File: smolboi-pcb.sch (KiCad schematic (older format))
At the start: 17 parts, among them U1 STM32F103C8Tx

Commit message: schematic before check
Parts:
- removed J?: USB_C_Receptacle_USB2.0, symbol Connector:USB_C_Receptacle_USB2.0
- added C? (x2): 1uF, symbol Device:C_Small
- added U?: XC6206, symbol random-keyboard-parts:XC6206
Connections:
- wire segments 80 -> 86
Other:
- note added: "USB_C Connector with ESD Protection"
- note added: "Voltage Step Down"
- moved on the sheet: C1, C2, C3, C4, C5, F?, R?, SW?, U1, U?, USB?

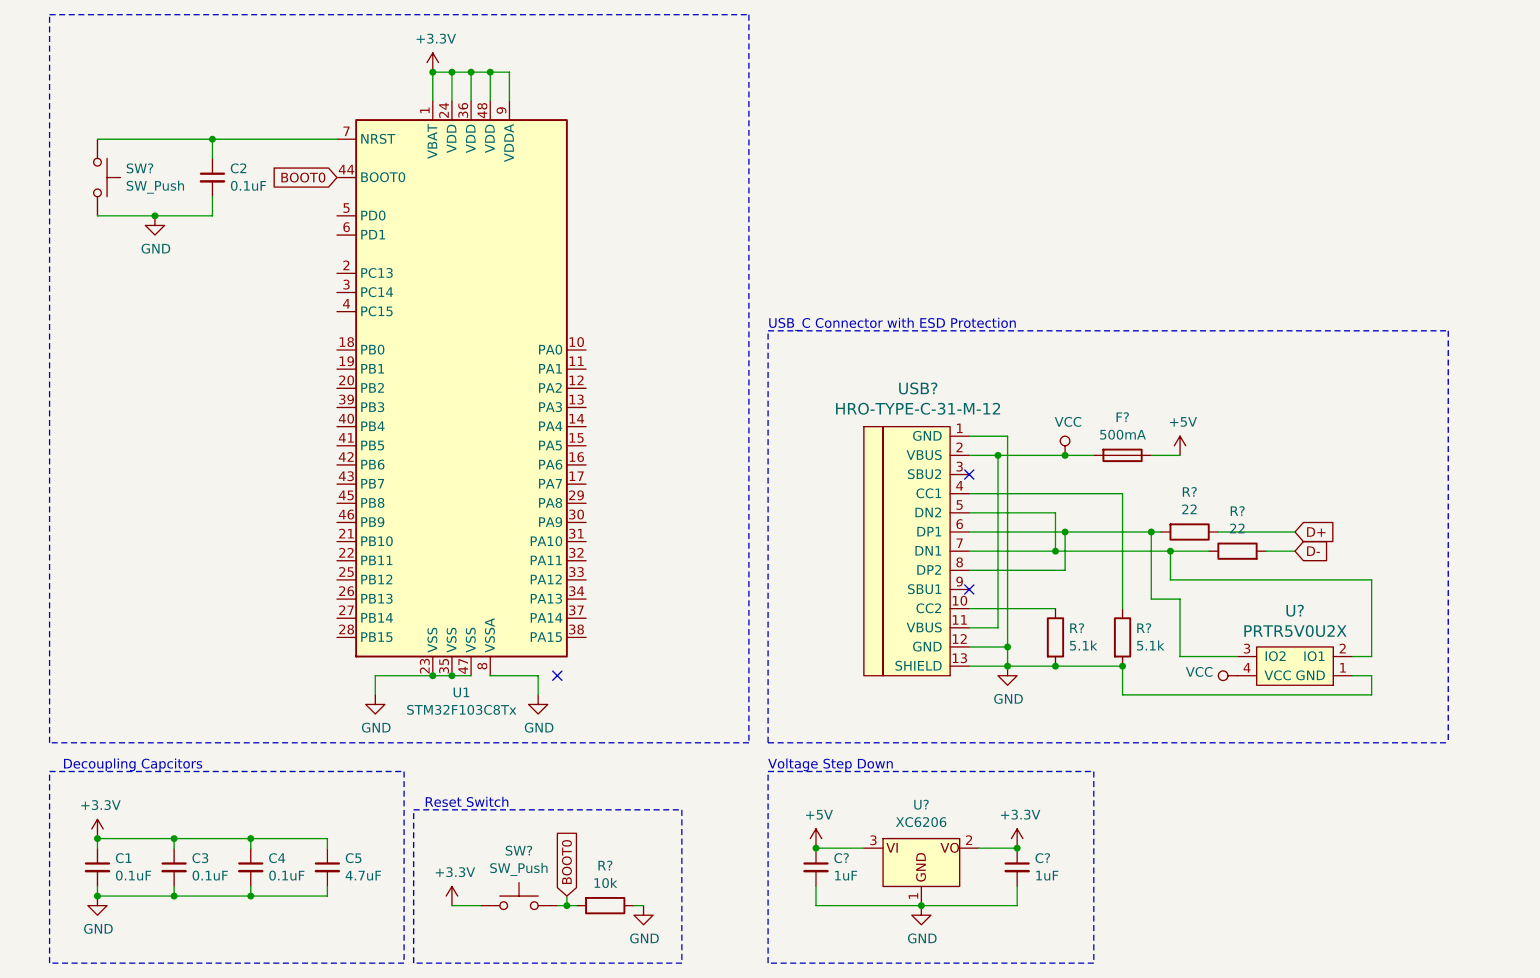
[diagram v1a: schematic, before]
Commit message: ceramic oscillator, major schematic modules finalized
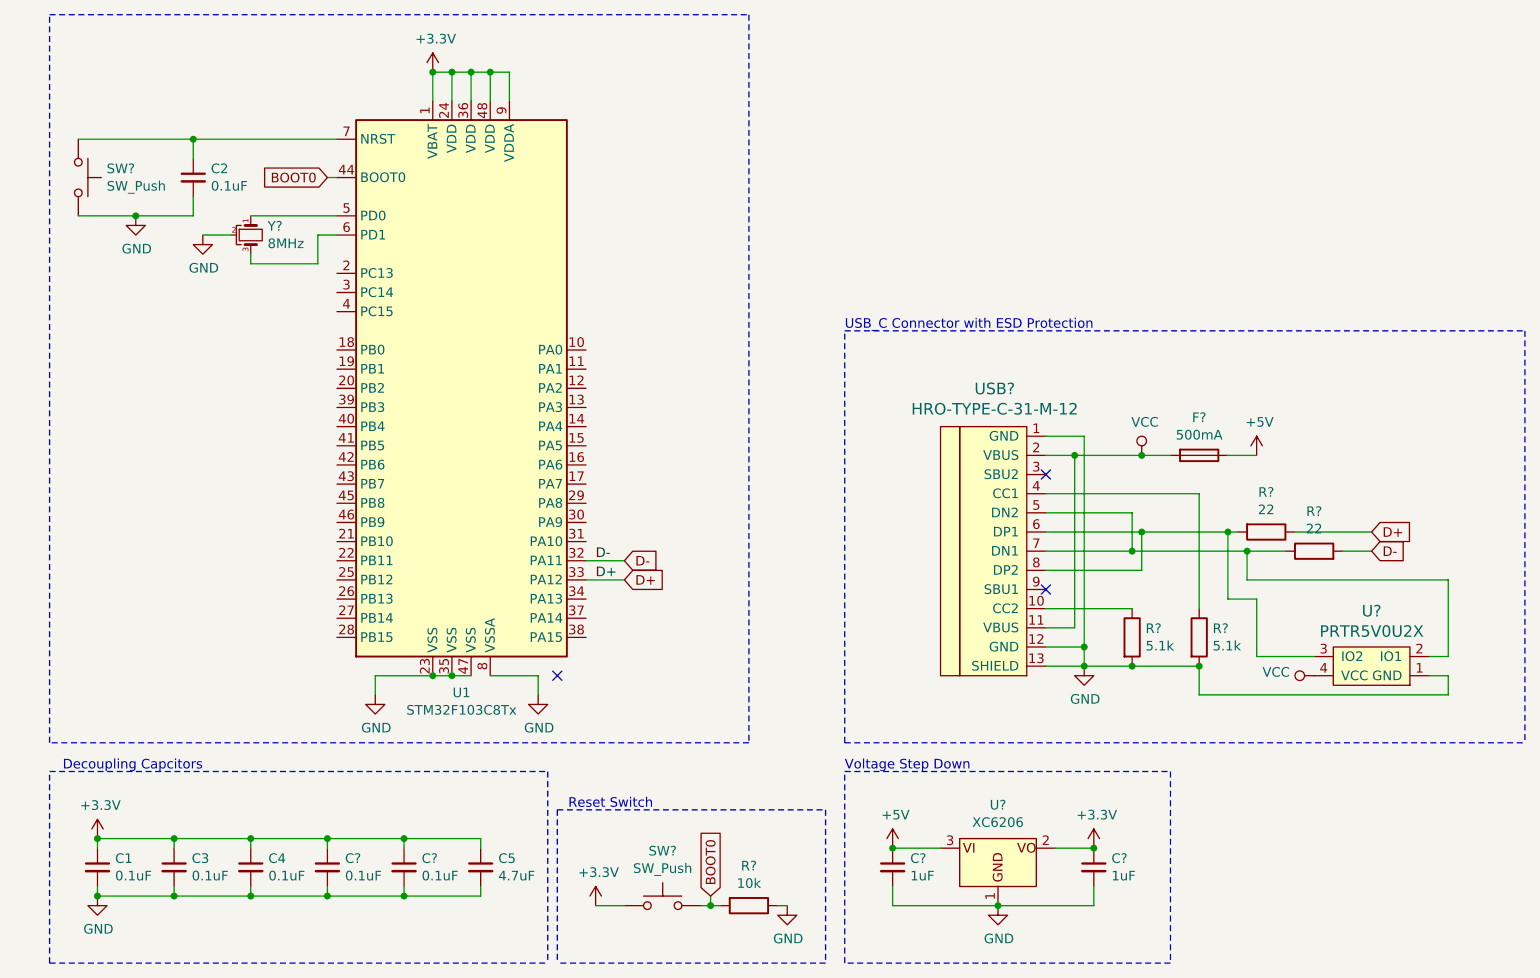
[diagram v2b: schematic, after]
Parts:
- added C? (x2): 0.1uF, symbol Device:C_Small
- added Y?: 8MHz, symbol Device:Crystal_GND2_Small
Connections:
- net +3V3: now also C?.1, C?.1
- net D+: now also U1.33 (PA12)
- net D-: now also U1.32 (PA11)
- net GND: now also C?.2, C?.2, Y?.2
- net at U1.5 (PD0): now also Y?.1
- net at U1.6 (PD1): now also Y?.3
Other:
- moved on the sheet: C2, C5, C?, F?, R?, SW?, U?, USB?

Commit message: up to finish diff pair routing
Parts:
- added D1, D10, D11, D12, D13, D14, D15, D16, D17, D18, D19, D2, D20, D21, D22, D23, D24, D25, D26, D27, D28, D29, D3, D30, D31, D32, D33, D34, D35, D36, D37, D38, D39, D4, D40, D41, D42, D43, D44, D45, D46, D5, D6, D7, D8, D9: D, Diode_SMD:D_SOD-123, symbol Device:D
- added SW1: ESC, MX_Only:MXOnly-1U-Hotswap, symbol Switch:SW_Push
- added SW10: O, MX_Only:MXOnly-1U-Hotswap, symbol Switch:SW_Push
- added SW11: P, MX_Only:MXOnly-1U-Hotswap, symbol Switch:SW_Push
- added SW12: Bksp, MX_Only:MXOnly-1U-Hotswap, symbol Switch:SW_Push
- added SW13: Tab, MX_Only:MXOnly-1U-Hotswap, symbol Switch:SW_Push
- added SW14: A, MX_Only:MXOnly-1U-Hotswap, symbol Switch:SW_Push
- added SW15: S, MX_Only:MXOnly-1U-Hotswap, symbol Switch:SW_Push
- added SW16: D, MX_Only:MXOnly-1U-Hotswap, symbol Switch:SW_Push
- added SW17: F, MX_Only:MXOnly-1U-Hotswap, symbol Switch:SW_Push
- added SW18: G, MX_Only:MXOnly-1U-Hotswap, symbol Switch:SW_Push
- added SW19: H, MX_Only:MXOnly-1U-Hotswap, symbol Switch:SW_Push
- added SW2: Q, MX_Only:MXOnly-1U-Hotswap, symbol Switch:SW_Push
- added SW20: J, MX_Only:MXOnly-1U-Hotswap, symbol Switch:SW_Push
- added SW21: K, MX_Only:MXOnly-1U-Hotswap, symbol Switch:SW_Push
- added SW22: L, MX_Only:MXOnly-1U-Hotswap, symbol Switch:SW_Push
- added SW23: ;, MX_Only:MXOnly-1U-Hotswap, symbol Switch:SW_Push
- added SW24: ', MX_Only:MXOnly-1U-Hotswap, symbol Switch:SW_Push
- added SW25: Shift, MX_Only:MXOnly-1U-Hotswap, symbol Switch:SW_Push
- added SW26: Z, MX_Only:MXOnly-1U-Hotswap, symbol Switch:SW_Push
- added SW27: X, MX_Only:MXOnly-1U-Hotswap, symbol Switch:SW_Push
- added SW28: C, MX_Only:MXOnly-1U-Hotswap, symbol Switch:SW_Push
- added SW29: V, MX_Only:MXOnly-1U-Hotswap, symbol Switch:SW_Push
- added SW3: W, MX_Only:MXOnly-1U-Hotswap, symbol Switch:SW_Push
- added SW30: B, MX_Only:MXOnly-1U-Hotswap, symbol Switch:SW_Push
- added SW31: N, MX_Only:MXOnly-1U-Hotswap, symbol Switch:SW_Push
- added SW32: M, MX_Only:MXOnly-1U-Hotswap, symbol Switch:SW_Push
- added SW33: ,, MX_Only:MXOnly-1U-Hotswap, symbol Switch:SW_Push
- added SW34: ., MX_Only:MXOnly-1U-Hotswap, symbol Switch:SW_Push
- added SW35: /, MX_Only:MXOnly-1U-Hotswap, symbol Switch:SW_Push
- added SW36: CpsLk, MX_Only:MXOnly-1U-Hotswap, symbol Switch:SW_Push
- added SW37: Ctrl, MX_Only:MXOnly-1U-Hotswap, symbol Switch:SW_Push
- added SW38: Win, MX_Only:MXOnly-1U-Hotswap, symbol Switch:SW_Push
- added SW39: Alt, MX_Only:MXOnly-1U-Hotswap, symbol Switch:SW_Push
- added SW4: E, MX_Only:MXOnly-1U-Hotswap, symbol Switch:SW_Push
- added SW40: FUP, MX_Only:MXOnly-1U-Hotswap, symbol Switch:SW_Push
- added SW41: FDN, MX_Only:MXOnly-1U-Hotswap, symbol Switch:SW_Push
- added SW42: Space, MX_Only:MXOnly-3U-Hotswap, symbol Switch:SW_Push
- added SW43: FRI, MX_Only:MXOnly-1U-Hotswap, symbol Switch:SW_Push
- added SW44: Left, MX_Only:MXOnly-1U-Hotswap, symbol Switch:SW_Push
- added SW45: Del, MX_Only:MXOnly-1U-Hotswap, symbol Switch:SW_Push
- added SW46: Enter, MX_Only:MXOnly-1U-Hotswap, symbol Switch:SW_Push
- added SW5: R, MX_Only:MXOnly-1U-Hotswap, symbol Switch:SW_Push
- added SW6: T, MX_Only:MXOnly-1U-Hotswap, symbol Switch:SW_Push
- added SW7: Y, MX_Only:MXOnly-1U-Hotswap, symbol Switch:SW_Push
- added SW8: U, MX_Only:MXOnly-1U-Hotswap, symbol Switch:SW_Push
- added SW9: I, MX_Only:MXOnly-1U-Hotswap, symbol Switch:SW_Push
- C1: renamed from C2; footprint (none) -> Capacitor_SMD:C_0402_1005Metric
- C2: renamed from C1; footprint (none) -> Capacitor_SMD:C_0402_1005Metric
- C3, C4: footprint (none) -> Capacitor_SMD:C_0402_1005Metric
- C5, C6, C8, C9: renamed from C?; footprint (none) -> Capacitor_SMD:C_0402_1005Metric
- C7: renamed from C5; footprint (none) -> Capacitor_SMD:C_0402_1005Metric
- F1: renamed from F?; footprint (none) -> Fuse:Fuse_1206_3216Metric
- R1, R2, R3, R4, R5: renamed from R?; footprint (none) -> Resistor_SMD:R_0402_1005Metric
- SW47, SW48: renamed from SW?; footprint (none) -> Button_Switch_SMD:SW_SPST_SKQG_WithStem
- U2: renamed from U?; footprint (none) -> random-keyboard-parts:SOT143B
- U3: renamed from U?; footprint (none) -> PMIC-LDO-XC6206P332MR-G_SOT23_:SOT-23
- USB1: renamed from USB?; footprint (none) -> Type-C:HRO-TYPE-C-31-M-12-Assembly
- Y1: renamed from Y?; footprint (none) -> CSTNE8M00GH5C000R0:OSC_CSTNE8M00GH5C000R0
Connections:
- net DN: now reaches R2.1, USB1.5 (DN2), USB1.7 (DN1)
- net DN: now also U2.3 (IO2); no longer U2.2 (IO1)
- net DP: now reaches R1.2, USB1.6 (DP1), USB1.8 (DP2)
- net DP: now also U2.2 (IO1); no longer U2.3 (IO2)
- new net: D1.2 (A), SW1.1
- new net: D2.2 (A), SW2.1
- new net: D3.2 (A), SW3.1
- new net: D4.2 (A), SW4.1
- new net: D5.2 (A), SW5.1
- new net: D6.2 (A), SW6.1
- new net: D7.2 (A), SW7.1
- new net: D8.2 (A), SW8.1
- new net: D9.2 (A), SW9.1
- new net: D10.2 (A), SW10.1
- new net: D11.2 (A), SW11.1
- new net: D12.2 (A), SW12.1
- new net: D13.2 (A), SW13.1
- new net: D14.2 (A), SW14.1
- new net: D15.2 (A), SW15.1
- new net: D16.2 (A), SW16.1
- new net: D17.2 (A), SW17.1
- new net: D18.2 (A), SW18.1
- new net: D19.2 (A), SW19.1
- new net: D20.2 (A), SW20.1
- new net: D21.2 (A), SW21.1
- new net: D22.2 (A), SW22.1
- new net: D23.2 (A), SW23.1
- new net: D24.2 (A), SW24.1
- new net: D25.2 (A), SW25.1
- new net: D26.2 (A), SW26.1
- new net: D27.2 (A), SW27.1
- new net: D28.2 (A), SW28.1
- new net: D29.2 (A), SW29.1
- new net: D30.2 (A), SW30.1
- new net: D31.2 (A), SW31.1
- new net: D32.2 (A), SW32.1
- new net: D33.2 (A), SW33.1
- new net: D34.2 (A), SW34.1
- new net: D35.2 (A), SW35.1
- new net: D36.2 (A), SW36.1
- new net: D37.2 (A), SW37.1
- new net: D38.2 (A), SW38.1
- new net: D39.2 (A), SW39.1
- new net: D40.2 (A), SW40.1
- new net: D41.2 (A), SW41.1
- new net: D42.2 (A), SW42.1
- new net: D43.2 (A), SW43.1
- new net: D44.2 (A), SW44.1
- new net: D45.2 (A), SW45.1
- new net: D46.2 (A), SW46.1
- new net col0: SW1.2, SW13.2, SW25.2, SW37.2
- new net col1: SW14.2, SW2.2, SW26.2, SW38.2
- new net col10: SW11.2, SW23.2, SW35.2, SW45.2
- new net col11: SW12.2, SW24.2, SW36.2, SW46.2
- new net col2: SW15.2, SW27.2, SW3.2, SW39.2
- new net col3: SW16.2, SW28.2, SW4.2, SW40.2
- new net col4: SW17.2, SW29.2, SW41.2, SW5.2
- new net col5: SW18.2, SW30.2, SW6.2
- new net col6: SW19.2, SW31.2, SW42.2, SW7.2
- new net col7: SW20.2, SW32.2, SW8.2
- new net col8: SW21.2, SW33.2, SW43.2, SW9.2
- new net col9: SW10.2, SW22.2, SW34.2, SW44.2
- new net row0: D1.1 (K), D10.1 (K), D11.1 (K), D12.1 (K), D2.1 (K), D3.1 (K), D4.1 (K), D5.1 (K), D6.1 (K), D7.1 (K), D8.1 (K), D9.1 (K)
- new net row1: D13.1 (K), D14.1 (K), D15.1 (K), D16.1 (K), D17.1 (K), D18.1 (K), D19.1 (K), D20.1 (K), D21.1 (K), D22.1 (K), D23.1 (K), D24.1 (K)
- new net row2: D25.1 (K), D26.1 (K), D27.1 (K), D28.1 (K), D29.1 (K), D30.1 (K), D31.1 (K), D32.1 (K), D33.1 (K), D34.1 (K), D35.1 (K), D36.1 (K)
- new net row3: D37.1 (K), D38.1 (K), D39.1 (K), D40.1 (K), D41.1 (K), D42.1 (K), D43.1 (K), D44.1 (K), D45.1 (K), D46.1 (K)
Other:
- note added: "08-21-2024"
- note added: "1.0\n"
- note added: "Smolboi PCB"
- moved on the sheet: C1, C2, C3, C4, C5, C6, C7, C8, C9, F1, R1, R2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

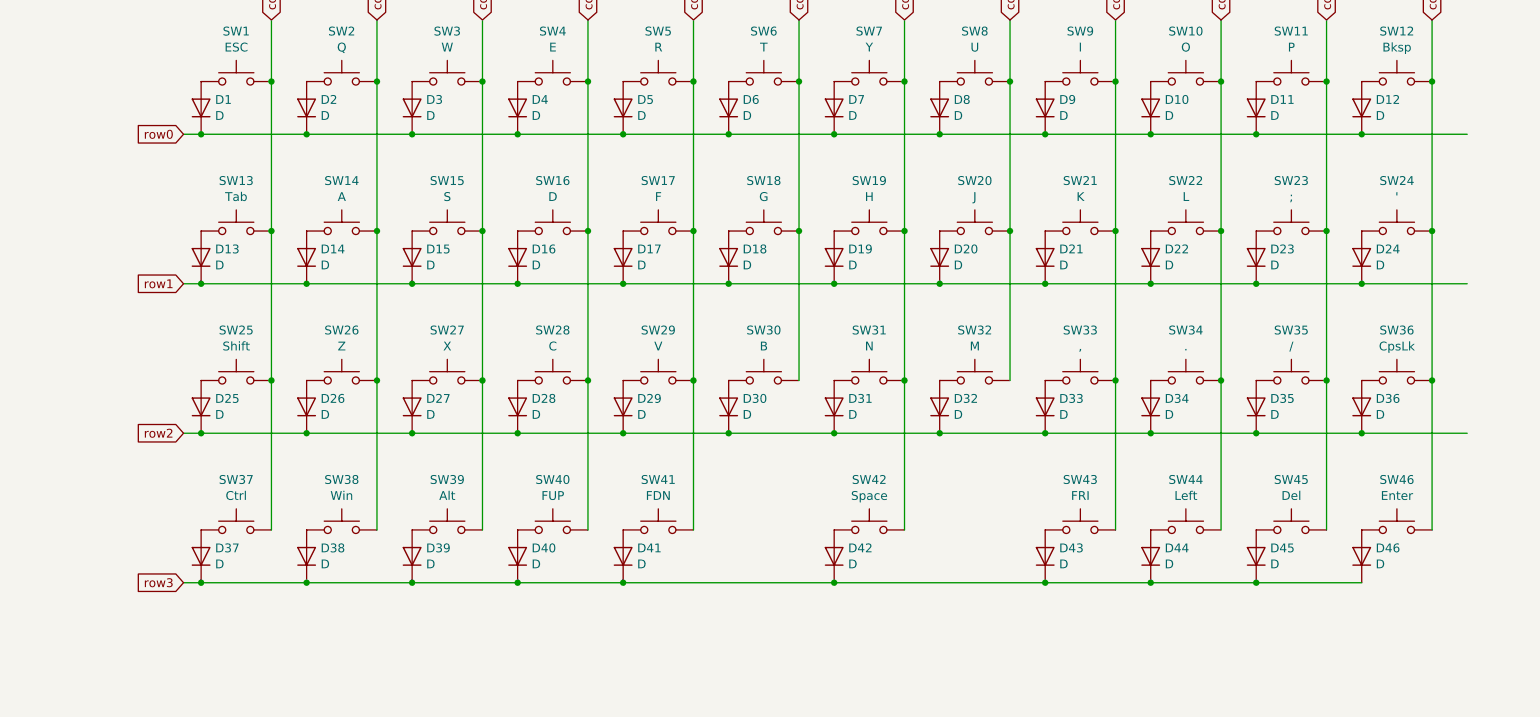
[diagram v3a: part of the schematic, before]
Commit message: staggered layout, routed diff pair on right side
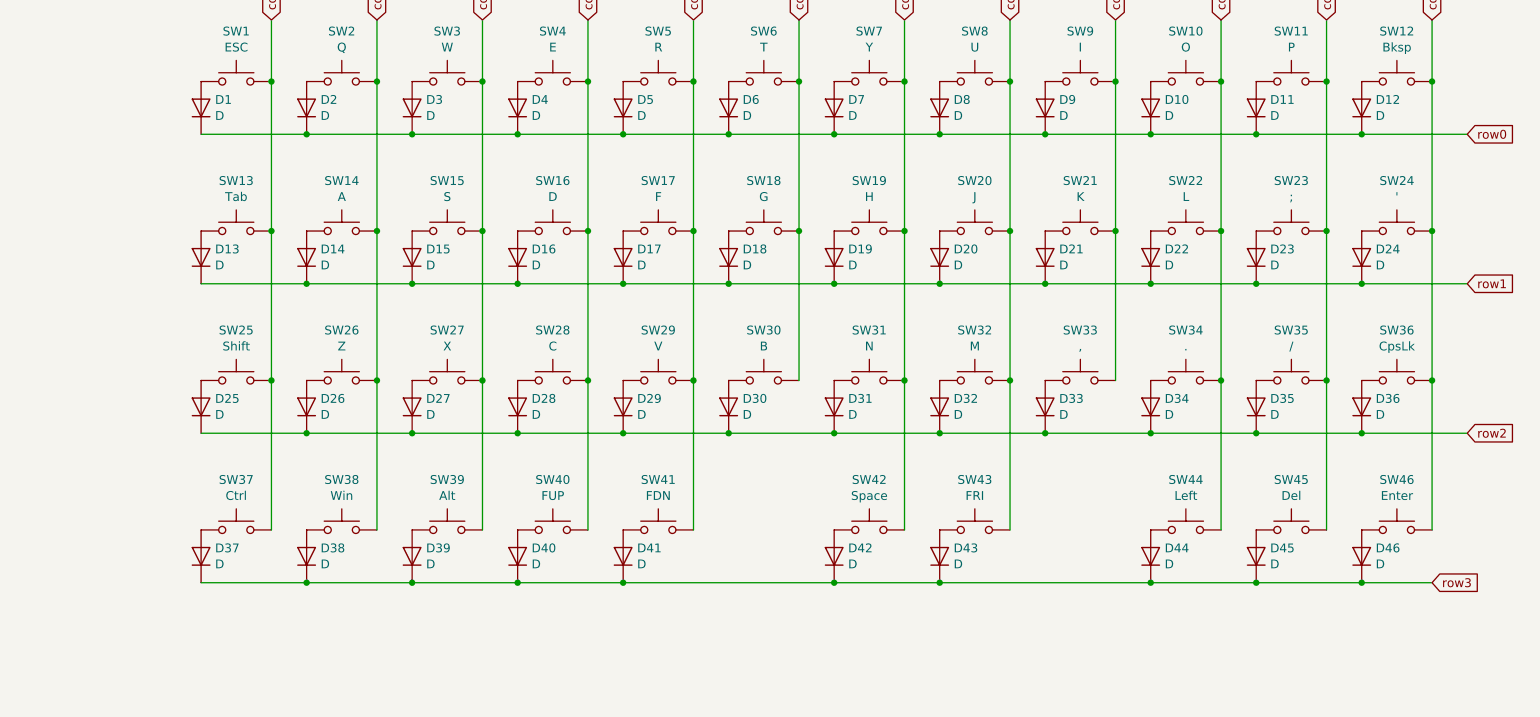
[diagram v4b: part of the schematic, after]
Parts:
- SW1, SW10, SW11, SW14, SW15, SW16, SW17, SW18, SW19, SW2, SW20, SW21, SW22, SW23, SW26, SW27, SW28, SW29, SW3, SW30, SW31, SW32, SW33, SW34, SW35, SW36, SW4, SW40, SW41, SW43, SW44, SW45, SW46, SW5, SW6, SW7, SW8, SW9: footprint MX_Only:MXOnly-1U-Hotswap -> MX_Only:MXOnly-1U-NoLED
- SW12, SW25: footprint MX_Only:MXOnly-1U-Hotswap -> MX_Only:MXOnly-1.75U-NoLED
- SW13, SW37, SW38, SW39: footprint MX_Only:MXOnly-1U-Hotswap -> MX_Only:MXOnly-1.25U-NoLED
- SW24: footprint MX_Only:MXOnly-1U-Hotswap -> MX_Only:MXOnly-1.5U-NoLED
- SW42: footprint MX_Only:MXOnly-3U-Hotswap -> MX_Only:MXOnly-2U-NoLED
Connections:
- net col7: now also SW43.2
- net col8: no longer SW43.2

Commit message: routed matrix
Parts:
- removed SW47: SW_Push, Button_Switch_SMD:SW_SPST_SKQG_WithStem, symbol Switch:SW_Push
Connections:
- net col0: now also U1.14 (PA4)
- net col1: now also U1.15 (PA5)
- net col10: now also U1.41 (PB5)
- net col11: now also U1.40 (PB4)
- net col2: now also U1.16 (PA6)
- net col3: now also U1.17 (PA7)
- net col4: now also U1.18 (PB0)
- net col5: now also U1.19 (PB1)
- net col6: now also U1.20 (PB2)
- net col7: now also U1.21 (PB10)
- net col8: now also U1.22 (PB11)
- net col9: now also U1.42 (PB6)
- net row0: now also U1.38 (PA15)
- net row1: now also U1.39 (PB3)
- net row2: now also U1.37 (PA14)
- net row3: now also U1.43 (PB7)
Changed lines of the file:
@@
 Wire Wire Line
 	2700 7650 2800 7650
-Connection ~ 1450 4850
 Wire Wire Line
 	1450 4850 2200 4850
 Wire Wire Line
 	1450 4850 1450 4950
-Wire Wire Line
-	850  4850 1450 4850
-Wire Wire Line
-	1150 5250 1450 5250
-Connection ~ 1150 5250
-Wire Wire Line
-	1450 5250 1450 5150
-Wire Wire Line
-	850  5250 1150 5250
-$Comp
-L Switch:SW_Push SW47
-U 1 1 66A6691F
-P 850 5050
-F 0 "SW47" V 804 5198 50  0000 L CNN
-F 1 "SW_Push" V 895 5198 50  0000 L CNN
-F 2 "Button_Switch_SMD:SW_SPST_SKQG_WithStem" H 850 5250 50  0001 C CNN
-F 3 "~" H 850 5250 50  0001 C CNN
-	1    850  5050
-	0    1    1    0
-$EndComp
 Text Notes 1500 8150 2    50   ~ 0
 Decoupling Capcitors
@@
 L power:GND #PWR02
 U 1 1 66A16F0D
-P 1150 5250
-F 0 "#PWR02" H 1150 5000 50  0001 C CNN
-F 1 "GND" H 1155 5077 50  0000 C CNN
-F 2 "" H 1150 5250 50  0001 C CNN
-F 3 "" H 1150 5250 50  0001 C CNN
-	1    1150 5250
+P 1450 5150
+F 0 "#PWR02" H 1450 4900 50  0001 C CNN
+F 1 "GND" H 1455 4977 50  0000 C CNN
+F 2 "" H 1450 5150 50  0001 C CNN
+F 3 "" H 1450 5150 50  0001 C CNN
+	1    1450 5150
 	1    0    0    -1
 $EndComp
@@
 	1    0    0    -1
 $EndComp
-Text GLabel 1450 6550 0    50   Input ~ 0
-col7
-Text GLabel 1450 6650 0    50   Input ~ 0
+Text GLabel 2200 7050 0    50   Input ~ 0
 col8
-Text GLabel 1450 6750 0    50   Input ~ 0
+Text GLabel 2200 6550 0    50   Input ~ 0
 col9
-Text GLabel 1450 6850 0    50   Input ~ 0
+Text GLabel 2200 6450 0    50   Input ~ 0
 col10
-Text GLabel 1450 6950 0    50   Input ~ 0
+Text GLabel 2200 6350 0    50   Input ~ 0
 col11
-Text GLabel 1450 7050 0    50   Input ~ 0
+Text GLabel 3500 7450 2    50   Input ~ 0
 row0
-Text GLabel 1450 5850 0    50   Input ~ 0
+Text GLabel 3500 6350 2    50   Input ~ 0
 col0
-Text GLabel 1450 5950 0    50   Input ~ 0
+Text GLabel 3500 6450 2    50   Input ~ 0
 col1
-Text GLabel 1450 6050 0    50   Input ~ 0
+Text GLabel 3500 6550 2    50   Input ~ 0
 col2
-Text GLabel 1450 6150 0    50   Input ~ 0
+Text GLabel 3500 6650 2    50   Input ~ 0
 col3
-Text GLabel 1450 6250 0    50   Input ~ 0
+Text GLabel 2200 5950 0    50   Input ~ 0
 col4
-Text GLabel 1450 6350 0    50   Input ~ 0
-col5
-Text GLabel 1450 6450 0    50   Input ~ 0
+Text GLabel 2200 6150 0    50   Input ~ 0
 col6
-Text GLabel 3600 6150 2    50   Input ~ 0
+Text GLabel 2200 6650 0    50   Input ~ 0
 row3
-Text GLabel 3600 6050 2    50   Input ~ 0
+Text GLabel 3500 7350 2    50   Input ~ 0
 row2
-Text GLabel 3600 5950 2    50   Input ~ 0
+Text GLabel 2200 6250 0    50   Input ~ 0
 row1
 Connection ~ 6350 7000
@@
 Wire Wire Line
 	9850 4450 11050 4450
+Text GLabel 2200 6950 0    50   Input ~ 0
+col7
+Text GLabel 2200 6050 0    50   Input ~ 0
+col5
 $EndSCHEMATC
